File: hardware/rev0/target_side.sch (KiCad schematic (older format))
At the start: 9 parts, among them IC1 ECP5-BGA256, U9 USB3343

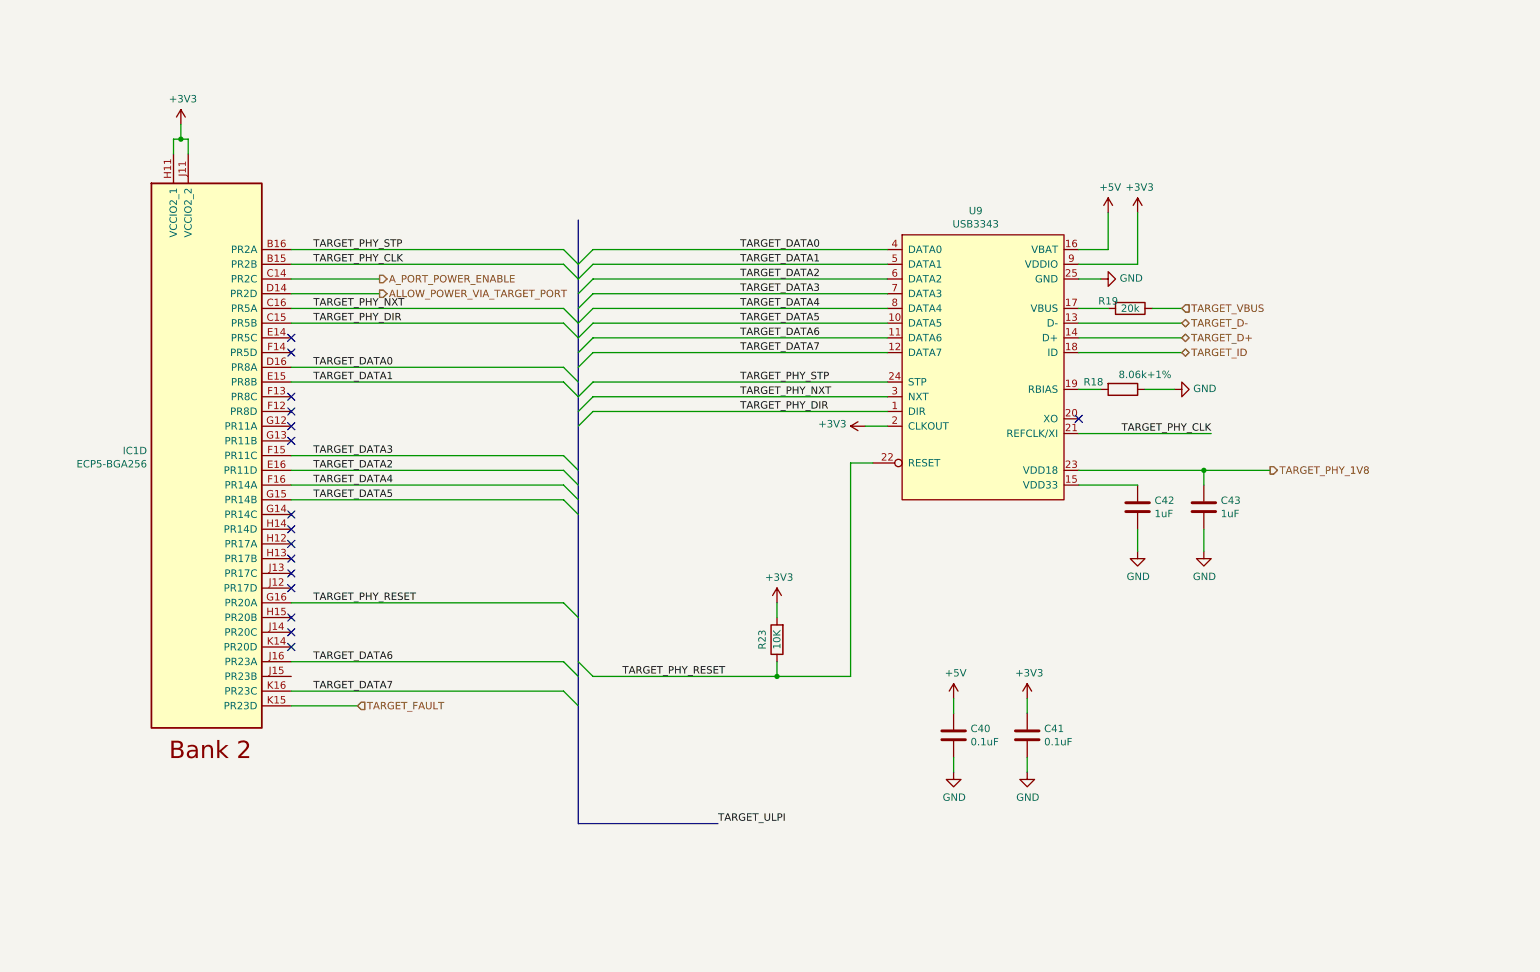
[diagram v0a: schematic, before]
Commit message: Remove target PHY
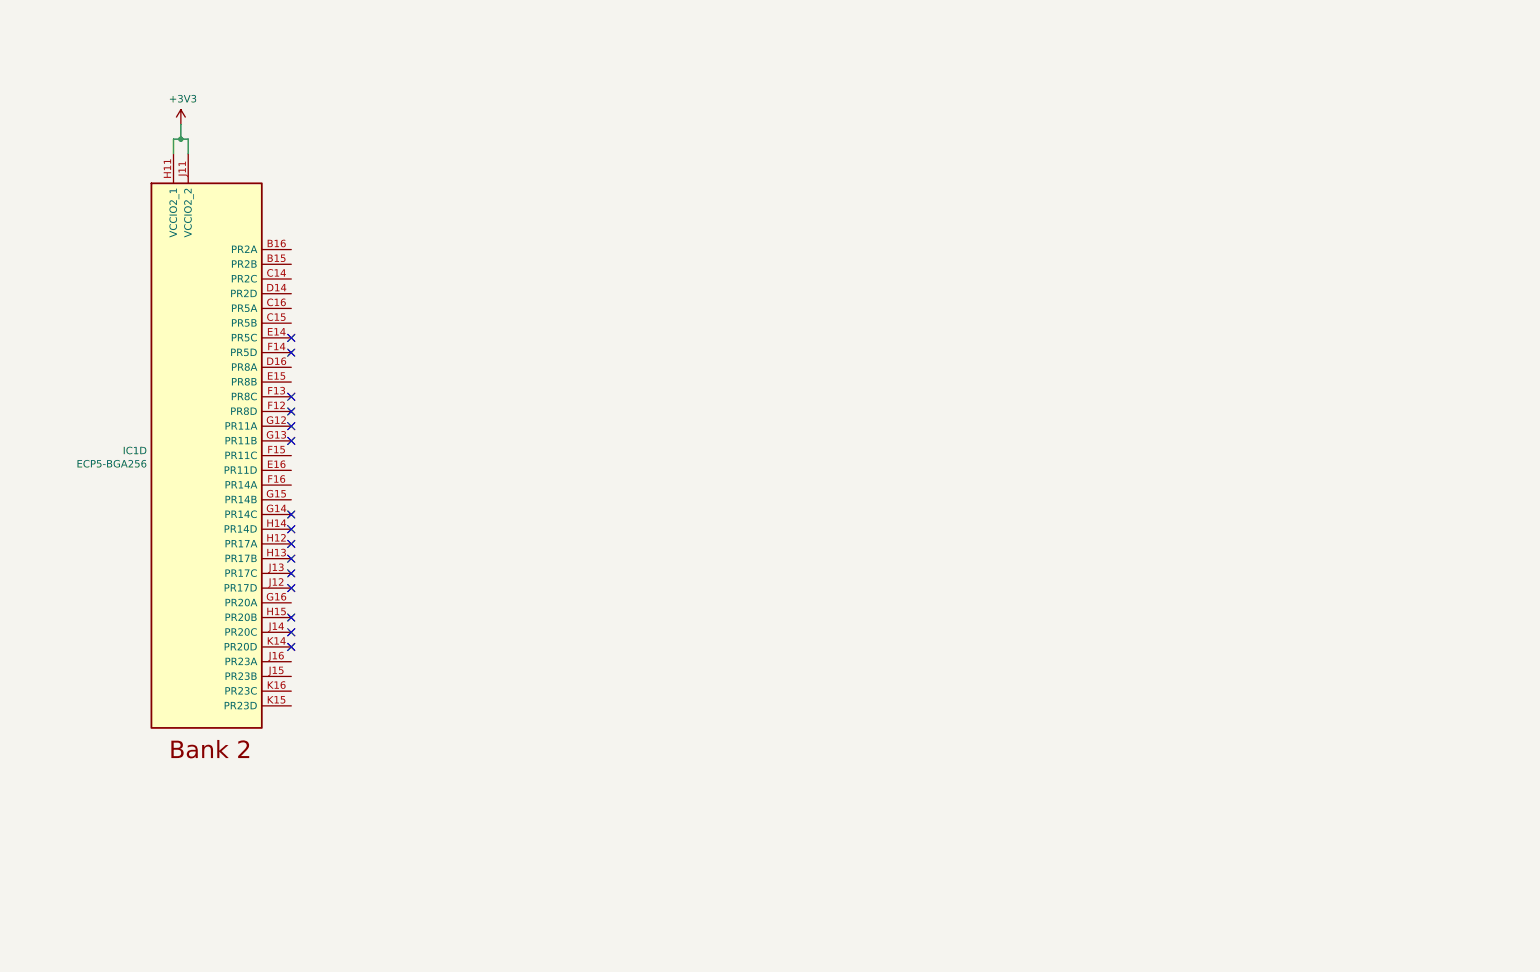
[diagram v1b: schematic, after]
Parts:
- removed C40, C41: 0.1uF, Capacitor_SMD:C_0402_1005Metric, symbol Device:C
- removed C42, C43: 1uF, Capacitor_SMD:C_0603_1608Metric, symbol Device:C
- removed R18: 8.06k+1%, Resistor_SMD:R_0402_1005Metric, symbol Device:R
- removed R19: 20k, Resistor_SMD:R_0402_1005Metric, symbol Device:R
- removed R23: 10K, Resistor_SMD:R_0402_1005Metric, symbol Device:R
- removed U9: USB3343, Package_DFN_QFN:VQFN-24-1EP_4x4mm_P0.5mm_EP2.45x2.45mm, symbol usb:USB3343
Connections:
- net ALLOW_POWER_VIA_TARGET_PORT: no longer names the net of IC1.D14 (PR2D)
- net A_PORT_POWER_ENABLE: no longer names the net of IC1.C14 (PR2C)
- net TARGET_DATA0: no longer names the net of IC1.D16 (PR8A)
- net TARGET_DATA1: no longer names the net of IC1.E15 (PR8B)
- net TARGET_DATA2: no longer names the net of IC1.E16 (PR11D)
- net TARGET_DATA3: no longer names the net of IC1.F15 (PR11C)
- net TARGET_DATA4: no longer names the net of IC1.F16 (PR14A)
- net TARGET_DATA5: no longer names the net of IC1.G15 (PR14B)
- net TARGET_DATA6: no longer names the net of IC1.J16 (PR23A)
- net TARGET_DATA7: no longer names the net of IC1.K16 (PR23C)
- net TARGET_FAULT: no longer names the net of IC1.K15 (PR23D)
- net TARGET_PHY_CLK: no longer names the net of IC1.B15 (PR2B)
- net TARGET_PHY_DIR: no longer names the net of IC1.C15 (PR5B)
- net TARGET_PHY_NXT: no longer names the net of IC1.C16 (PR5A)
- net TARGET_PHY_RESET: no longer names the net of IC1.G16 (PR20A)
- net TARGET_PHY_STP: no longer names the net of IC1.B16 (PR2A)
- no-connect marks 16 -> 15

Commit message: Add AT86RF215 & some schematic hookup
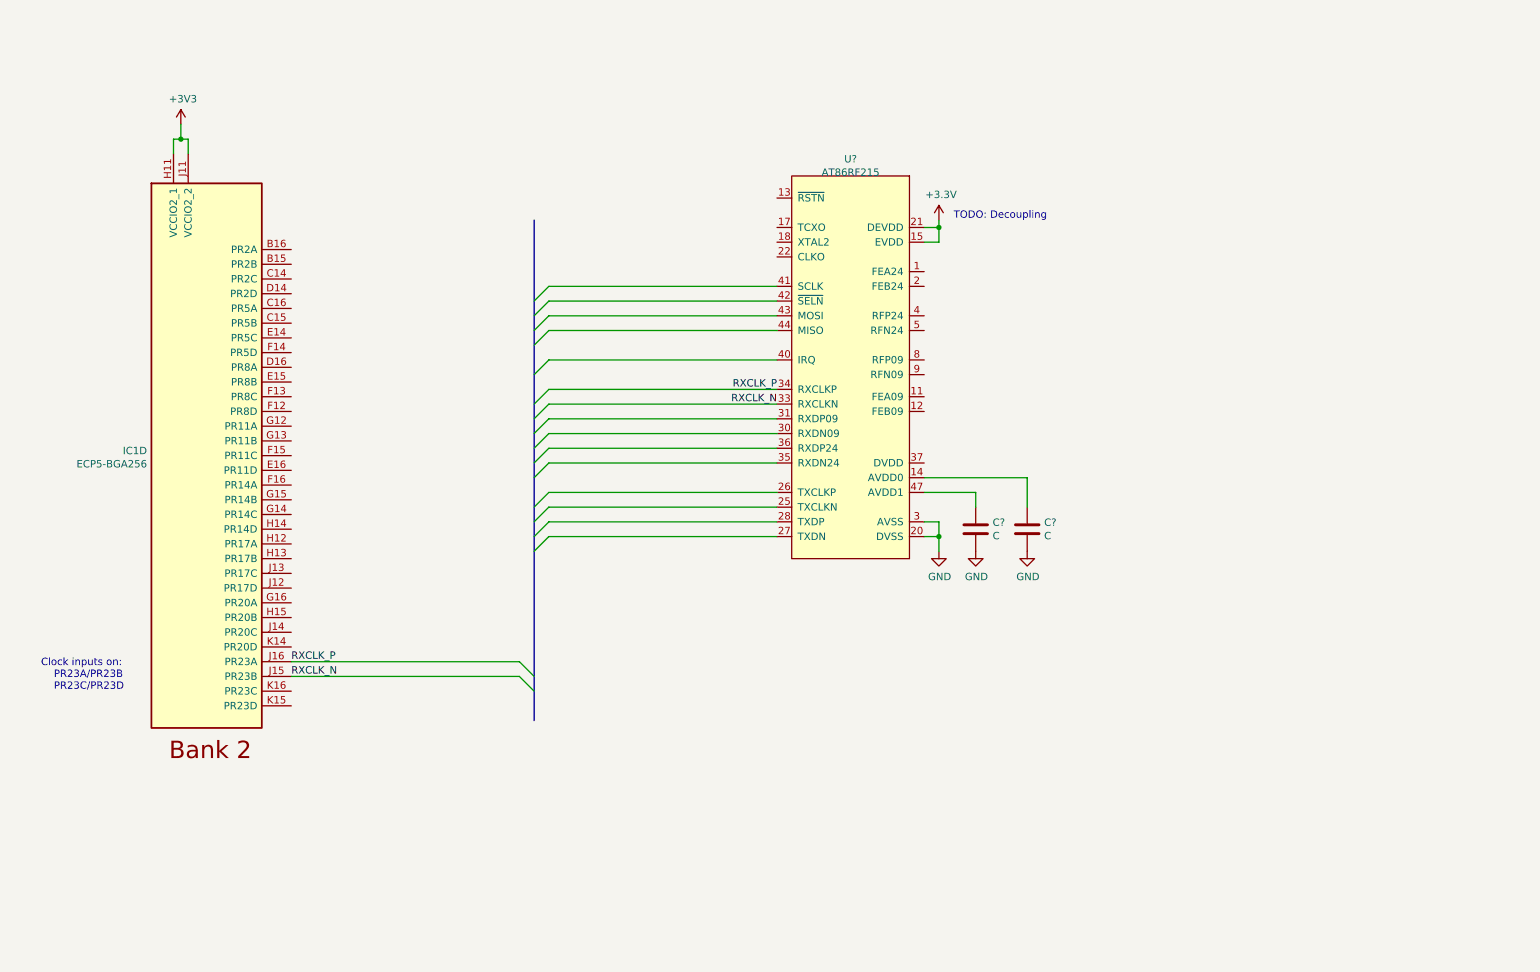
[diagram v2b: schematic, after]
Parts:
- added C? (x2): C, symbol Device:C
- added U?: AT86RF215, symbol rf:AT86RF215
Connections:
- net +3V3: now also U?.15 (EVDD), U?.21 (DEVDD), U?.29 (DEVDD), U?.39 (DEVDD), U?.46 (EVDD)
- net RXCLK_N: now reaches IC1.J15 (PR23B)
- net RXCLK_N: now also U?.33 (RXCLKN)
- net RXCLK_P: now reaches IC1.J16 (PR23A)
- net RXCLK_P: now also U?.34 (RXCLKP)
- new net: C?.1, U?.14 (AVDD0)
- new net: C?.1, U?.47 (AVDD1)
- new net AVSS: C?.2, C?.2, U?.10 (AVSS), U?.16 (AVSS), U?.19 (AVSS), U?.20 (DVSS), U?.23 (DVSS), U?.24 (DVSS), U?.3 (AVSS), U?.32 (DVSS), U?.38 (DVSS), U?.45 (AVSS), U?.48 (AVSS), U?.49 (AVSS), U?.6 (AVSS), U?.7 (AVSS)
- no-connect marks 15 -> 0
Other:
- note added: "Clock inputs on:\n PR23A/PR23B\n PR23C/PR23D"
- note added: "TODO: Decoupling\n"
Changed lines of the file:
@@
 	1    0    0    -1
 $EndComp
-NoConn ~ 2600 3550
-NoConn ~ 2600 3150
-NoConn ~ 2600 3250
-NoConn ~ 2600 3650
-NoConn ~ 2600 3750
-NoConn ~ 2600 3850
-NoConn ~ 2600 4350
-NoConn ~ 2600 4450
-NoConn ~ 2600 4550
-NoConn ~ 2600 4650
-NoConn ~ 2600 4750
-NoConn ~ 2600 4850
-NoConn ~ 2600 5050
-NoConn ~ 2600 5150
-NoConn ~ 2600 5250
 Wire Wire Line
 	1800 1900 1800 1800
@@
 	1    0    0    -1
 $EndComp
+$Comp
+L rf:AT86RF215 U?
+U 1 1 5E8BDF16
+P 6400 3350
+F 0 "U?" H 6400 4765 50  0000 C CNN
+F 1 "AT86RF215" H 6400 4674 50  0000 C CNN
+F 2 "" H 6400 3100 50  0001 C CNN
+F 3 "" H 6400 3100 50  0001 C CNN
+	1    6400 3350
+	1    0    0    -1
+$EndComp
+Entry Wire Line
+	4250 3200 4350 3100
+Entry Wire Line
+	4250 3000 4350 2900
+Entry Wire Line
+	4250 2900 4350 2800
+Wire Wire Line
+	4350 2900 5900 2900
+Wire Wire Line
+	4350 2800 5900 2800
+Wire Wire Line
+	5900 3000 4350 3000
+Wire Wire Line
+	5900 3100 4350 3100
+Entry Wire Line
+	4350 3000 4250 3100
+Wire Wire Line
+	5900 3300 4350 3300
+Wire Wire Line
+	5900 3500 4350 3500
+Wire Wire Line
+	5900 3600 4350 3600
+Wire Wire Line
+	5900 3700 4350 3700
+Wire Wire Line
+	5900 3800 4350 3800
+Wire Wire Line
+	5900 3900 4350 3900
+Wire Wire Line
+	5900 4000 4350 4000
+Wire Wire Line
+	5900 4200 4350 4200
+Wire Wire Line
+	5900 4300 4350 4300
+Wire Wire Line
+	5900 4400 4350 4400
+Wire Wire Line
+	5900 4500 4350 4500
+Entry Wire Line
+	4250 3400 4350 3300
+Entry Wire Line
+	4250 3600 4350 3500
+Entry Wire Line
+	4250 3700 4350 3600
+Entry Wire Line
+	4250 3800 4350 3700
+Entry Wire Line
+	4250 3900 4350 3800
+Entry Wire Line
+	4250 4000 4350 3900
+Entry Wire Line
+	4250 4100 4350 4000
+Entry Wire Line
+	4250 4300 4350 4200
+Entry Wire Line
+	4250 4400 4350 4300
+Entry Wire Line
+	4250 4500 4350 4400
+Entry Wire Line
+	4250 4600 4350 4500
+$Comp
+L power:GND #PWR?
+U 1 1 5E8DC56B
+P 7000 4600
+F 0 "#PWR?" H 7000 4350 50  0001 C CNN
+F 1 "GND" H 7005 4427 50  0000 C CNN
+F 2 "" H 7000 4600 50  0001 C CNN
+F 3 "" H 7000 4600 50  0001 C CNN
+	1    7000 4600
+	1    0    0    -1
+$EndComp
+Wire Wire Line
+	6900 4500 7000 4500
+Wire Wire Line
+	7000 4500 7000 4600
+Wire Wire Line
+	6900 4400 7000 4400
+Wire Wire Line
+	7000 4400 7000 4500
+Connection ~ 7000 4500
+$Comp
+L Device:C C?
+U 1 1 5E8DD3C4
+P 7250 4450
+F 0 "C?" H 7365 4496 50  0000 L CNN
+F 1 "C" H 7365 4405 50  0000 L CNN
+F 2 "" H 7288 4300 50  0001 C CNN
+F 3 "~" H 7250 4450 50  0001 C CNN
+	1    7250 4450
+	1    0    0    -1
+$EndComp
+$Comp
+L Device:C C?
+U 1 1 5E8DDA59
+P 7600 4450
+F 0 "C?" H 7715 4496 50  0000 L CNN
+F 1 "C" H 7715 4405 50  0000 L CNN
+F 2 "" H 7638 4300 50  0001 C CNN
+F 3 "~" H 7600 4450 50  0001 C CNN
+	1    7600 4450
+	1    0    0    -1
+$EndComp
+$Comp
+L power:GND #PWR?
+U 1 1 5E8DDC6A
+P 7250 4600
+F 0 "#PWR?" H 7250 4350 50  0001 C CNN
+F 1 "GND" H 7255 4427 50  0000 C CNN
+F 2 "" H 7250 4600 50  0001 C CNN
+F 3 "" H 7250 4600 50  0001 C CNN
+	1    7250 4600
+	1    0    0    -1
+$EndComp
+$Comp
+L power:GND #PWR?
+U 1 1 5E8DDD8B
+P 7600 4600
+F 0 "#PWR?" H 7600 4350 50  0001 C CNN
+F 1 "GND" H 7605 4427 50  0000 C CNN
+F 2 "" H 7600 4600 50  0001 C CNN
+F 3 "" H 7600 4600 50  0001 C CNN
+	1    7600 4600
+	1    0    0    -1
+$EndComp
+Wire Wire Line
+	6900 4200 7250 4200
+Wire Wire Line
+	7250 4200 7250 4300
+Wire Wire Line
+	6900 4100 7600 4100
+Wire Wire Line
+	7600 4100 7600 4300
+$Comp
+L power:+3.3V #PWR?
+U 1 1 5E8F94BD
+P 7000 2350
+F 0 "#PWR?" H 7000 2200 50  0001 C CNN
+F 1 "+3.3V" H 7015 2523 50  0000 C CNN
+F 2 "" H 7000 2350 50  0001 C CNN
+F 3 "" H 7000 2350 50  0001 C CNN
+	1    7000 2350
+	1    0    0    -1
+$EndComp
+Wire Wire Line
+	6900 2400 7000 2400
+Wire Wire Line
+	7000 2400 7000 2350
+Wire Wire Line
+	6900 2500 7000 2500
+Wire Wire Line
+	7000 2500 7000 2400
+Connection ~ 7000 2400
+Text Notes 7100 2350 0    50   ~ 0
+TODO: Decoupling\n
+Text Label 5900 3500 2    50   ~ 0
+RXCLK_P
+Text Label 5900 3600 2    50   ~ 0
+RXCLK_N
+Text Notes 900  5550 0    50   ~ 0
+Clock inputs on:\n    PR23A/PR23B\n    PR23C/PR23D
+Text Label 2600 5350 0    50   ~ 0
+RXCLK_P
+Text Label 2600 5450 0    50   ~ 0
+RXCLK_N
+Wire Wire Line
+	2600 5350 4150 5350
+Wire Wire Line
+	2600 5450 4150 5450
+Wire Bus Line
+	4250 2350 4250 5750
+Entry Wire Line
+	4150 5350 4250 5450
+Entry Wire Line
+	4150 5450 4250 5550
 $EndSCHEMATC
